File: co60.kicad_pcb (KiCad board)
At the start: 2 copper layers, 285 x 95.1 mm, 251 parts, among them J1 Conn_01x06, Q1 PZT2222A, SW1 SW_Push, U1 ATMEGA32U4, Y1 16MHz

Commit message: Update: Move some components on PCB
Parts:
- moved D14 1.33 mm to (344.7, 57.1)
- moved D1 0.78 mm to (84.8, 55.9)
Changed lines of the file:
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@@
   )
   (module Diodes_SMD:D_SOD-123 (layer B.Cu)
-    (at 344.090625 55.959375 90)
+    (at 344.678 57.15 90)
     (descr SOD-123)
     (tags SOD-123)
@@
   )
   (module Diodes_SMD:D_SOD-123 (layer B.Cu)
-    (at 84.9 55.1)
-    (descr SOD-123)
-    (tags SOD-123)
+    (at 84.836 55.88)
+    (descr SOD-123)
+    (tags SOD-123)

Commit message: Update: Rename some components
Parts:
- renumbered R_MCU_3 to RC2, R_MCU_4 to RC3, R_USB_1 to RC4, R_USB_2 to RC5, R_USB_3 to RC6, R_USB_4 to RC7
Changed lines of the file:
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@@
   (net 98 "Net-(Q1-Pad1)")
   (net 99 LEDPWM)
-  (net 100 "Net-(R_MCU_3-Pad1)")
+  (net 100 "Net-(RC2-Pad1)")
   (net 101 D_PLUS)
   (net 102 D_MINUS)
@@
   (net 176 "Net-(K_\\1-Pad4)")
   (net 177 "Net-(K_]1-Pad4)")
-  (net 178 "Net-(R_USB_3-Pad2)")
-  (net 179 "Net-(R_USB_4-Pad2)")
+  (net 178 "Net-(RC6-Pad2)")
+  (net 179 "Net-(RC7-Pad2)")
   (net 180 "Net-(USB1-PadB8)")
   (net 181 "Net-(USB1-PadB10)")
@@
     (add_net "Net-(K_]1-Pad4)")
     (add_net "Net-(Q1-Pad1)")
-    (add_net "Net-(R_MCU_3-Pad1)")
-    (add_net "Net-(R_USB_3-Pad2)")
-    (add_net "Net-(R_USB_4-Pad2)")
+    (add_net "Net-(RC2-Pad1)")
+    (add_net "Net-(RC6-Pad2)")
+    (add_net "Net-(RC7-Pad2)")
     (add_net "Net-(U1-Pad36)")
     (add_net "Net-(U1-Pad37)")
@@
       (net 1 GND))
     (pad B5 smd rect (at 0.5 -1.04) (size 0.3 0.7) (layers B.Cu B.Paste B.Mask)
-      (net 179 "Net-(R_USB_4-Pad2)"))
+      (net 179 "Net-(RC7-Pad2)"))
     (pad B4 smd rect (at 1 -1.04) (size 0.3 0.7) (layers B.Cu B.Paste B.Mask)
       (net 110 "Net-(DP1-Pad4)"))
@@
       (net 79 "Net-(DP1-Pad2)"))
     (pad A5 smd rect (at -0.75 0.66) (size 0.3 0.7) (layers B.Cu B.Paste B.Mask)
-      (net 178 "Net-(R_USB_3-Pad2)"))
+      (net 178 "Net-(RC6-Pad2)"))
     (pad A10 smd rect (at 1.75 0.66) (size 0.3 0.7) (layers B.Cu B.Paste B.Mask)
       (net 186 "Net-(USB1-PadA10)"))
@@
       (net 84 COL3))
     (pad 33 smd oval (at 5.715 4.0005 270) (size 1.89992 0.4064) (layers B.Cu B.Paste B.Mask)
-      (net 100 "Net-(R_MCU_3-Pad1)"))
+      (net 100 "Net-(RC2-Pad1)"))
     (pad 1 smd oval (at -5.715 4.0005 270) (size 1.89992 0.4064) (layers B.Cu B.Paste B.Mask)
       (net 83 COL2))
@@
     (tags "resistor 0603")
     (attr smd)
-    (fp_text reference R_USB_4 (at 0 1.45 90) (layer B.SilkS)
+    (fp_text reference RC7 (at 0 1.45 90) (layer B.SilkS)
       (effects (font (size 1 1) (thickness 0.15)) (justify mirror))
     )
@@
       (net 1 GND))
     (pad 2 smd rect (at 0.75 0 90) (size 0.5 0.9) (layers B.Cu B.Paste B.Mask)
-      (net 179 "Net-(R_USB_4-Pad2)"))
+      (net 179 "Net-(RC7-Pad2)"))
     (model ${KISYS3DMOD}/Resistors_SMD.3dshapes/R_0603.wrl
       (at (xyz 0 0 0))
@@
     (tags "resistor 0603")
     (attr smd)
-    (fp_text reference R_USB_3 (at 0 1.45 270) (layer B.SilkS)
+    (fp_text reference RC6 (at 0 1.45 270) (layer B.SilkS)
       (effects (font (size 1 1) (thickness 0.15)) (justify mirror))
     )
@@
       (net 1 GND))
     (pad 2 smd rect (at 0.75 0 270) (size 0.5 0.9) (layers B.Cu B.Paste B.Mask)
-      (net 178 "Net-(R_USB_3-Pad2)"))
+      (net 178 "Net-(RC6-Pad2)"))
     (model ${KISYS3DMOD}/Resistors_SMD.3dshapes/R_0603.wrl
       (at (xyz 0 0 0))
@@
     (tags "resistor 0603")
     (attr smd)
-    (fp_text reference R_USB_2 (at 0 1.45 90) (layer B.SilkS)
+    (fp_text reference RC5 (at 0 1.45 90) (layer B.SilkS)
       (effects (font (size 1 1) (thickness 0.15)) (justify mirror))
     )
@@
     (tags "resistor 0603")
     (attr smd)
-    (fp_text reference R_USB_1 (at 0 1.45 90) (layer B.SilkS)
+    (fp_text reference RC4 (at 0 1.45 90) (layer B.SilkS)
       (effects (font (size 1 1) (thickness 0.15)) (justify mirror))
     )
@@
     (tags "resistor 0603")
     (attr smd)
-    (fp_text reference R_MCU_4 (at 0 1.45) (layer B.SilkS)
+    (fp_text reference RC3 (at 0 1.45) (layer B.SilkS)
       (effects (font (size 1 1) (thickness 0.15)) (justify mirror))
     )
@@
     (tags "resistor 0603")
     (attr smd)
-    (fp_text reference R_MCU_3 (at 0 1.45 180) (layer B.SilkS)
+    (fp_text reference RC2 (at 0 1.45 180) (layer B.SilkS)
       (effects (font (size 1 1) (thickness 0.15)) (justify mirror))
     )
@@
     (fp_line (start 1.25 -0.7) (end -1.25 -0.7) (layer B.CrtYd) (width 0.05))
     (pad 1 smd rect (at -0.75 0 180) (size 0.5 0.9) (layers B.Cu B.Paste B.Mask)
-      (net 100 "Net-(R_MCU_3-Pad1)"))
+      (net 100 "Net-(RC2-Pad1)"))
     (pad 2 smd rect (at 0.75 0 180) (size 0.5 0.9) (layers B.Cu B.Paste B.Mask)
       (net 1 GND))

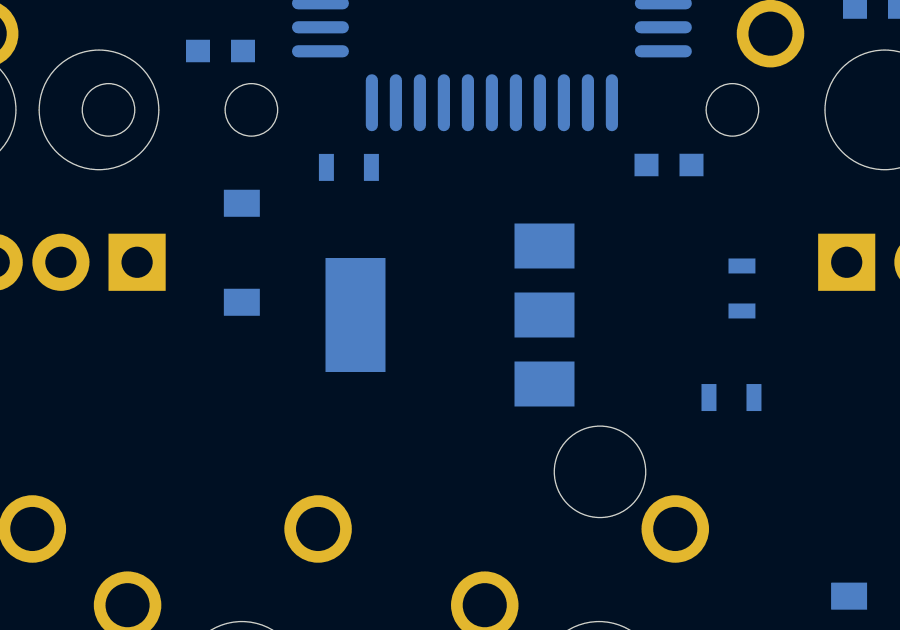
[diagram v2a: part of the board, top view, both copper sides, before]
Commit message: Update: Switch transistor to something smaller
I don't think I needed a transistor as big as I had for the
LEDs. I've switched to a SOT-23 footprint BJT that can
dissipate 500 mW. This should be more than enough for
68 LEDs at 5 mA each.
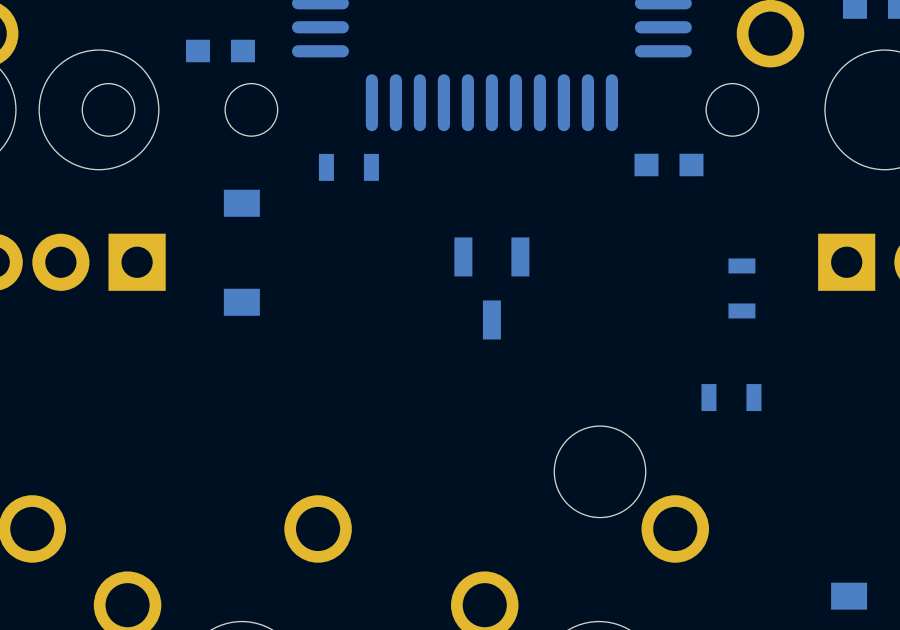
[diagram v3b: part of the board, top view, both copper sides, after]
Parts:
- Q1: value PZT2222A -> FMMT493TA; footprint TO_SOT_Packages_SMD:SOT-223 -> digikey-footprints:SOT-23-3
- moved Q1 1.65 mm to (108.3, 106.0), turned to 270 degrees
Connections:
- Q1 pad 1: Net-(Q1-Pad1) -> GND
- Q1 pad 2: LEDGND -> Net-(Q1-Pad2)
- Q1 pad 3: GND -> LEDGND
- RC1 pad 1: Net-(Q1-Pad1) -> Net-(Q1-Pad2)

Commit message: Update: More PCB component adjustment
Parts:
- K_LCTL1: footprint MX_Alps_Hybrid:MXOnly-1.25U -> MX_Alps_Hybrid:MXOnly-1.25U-FLIPPED
- K_LCTL2: footprint MX_Alps_Hybrid:MXOnly-1.5U-FLIPPED -> MX_Alps_Hybrid:MXOnly-1.5U
- moved C8 4.97 mm to (98.8, 88.1), turned to 90 degrees
- moved C3 2.50 mm to (109.5, 84.5), turned to 90 degrees
- moved C5 1.70 mm to (98.8, 91.7), turned to 270 degrees
- moved RC2 1.65 mm to (103.6, 103.6)
- moved R30 1.19 mm to (86.9, 103.6)
- moved C4 0.77 mm to (118.1, 90.4)
- moved RC3 0.70 mm to (115.6, 88.4)
- moved C6 0.64 mm to (98.8, 97.6)
- moved USB1 0.14 mm to (97.2, 59.7)

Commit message: Update: Reverse crystal connections
I'm not sure if this matters or not, but it seems
consistent with the way the GH60 does it.
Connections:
- U1 pad 16: Net-(C1-Pad1) -> Net-(C2-Pad1)
- U1 pad 17: Net-(C2-Pad1) -> Net-(C1-Pad1)
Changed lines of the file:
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@@
       (net 5 VCC))
     (pad 17 smd oval (at 0 -5.715 270) (size 0.4064 1.89992) (layers B.Cu B.Paste B.Mask)
+      (net 2 "Net-(C1-Pad1)"))
+    (pad 16 smd oval (at -0.8001 -5.715 270) (size 0.4064 1.89992) (layers B.Cu B.Paste B.Mask)
       (net 3 "Net-(C2-Pad1)"))
-    (pad 16 smd oval (at -0.8001 -5.715 270) (size 0.4064 1.89992) (layers B.Cu B.Paste B.Mask)
-      (net 2 "Net-(C1-Pad1)"))
     (pad 15 smd oval (at -1.6002 -5.715 270) (size 0.4064 1.89992) (layers B.Cu B.Paste B.Mask)
       (net 1 GND))

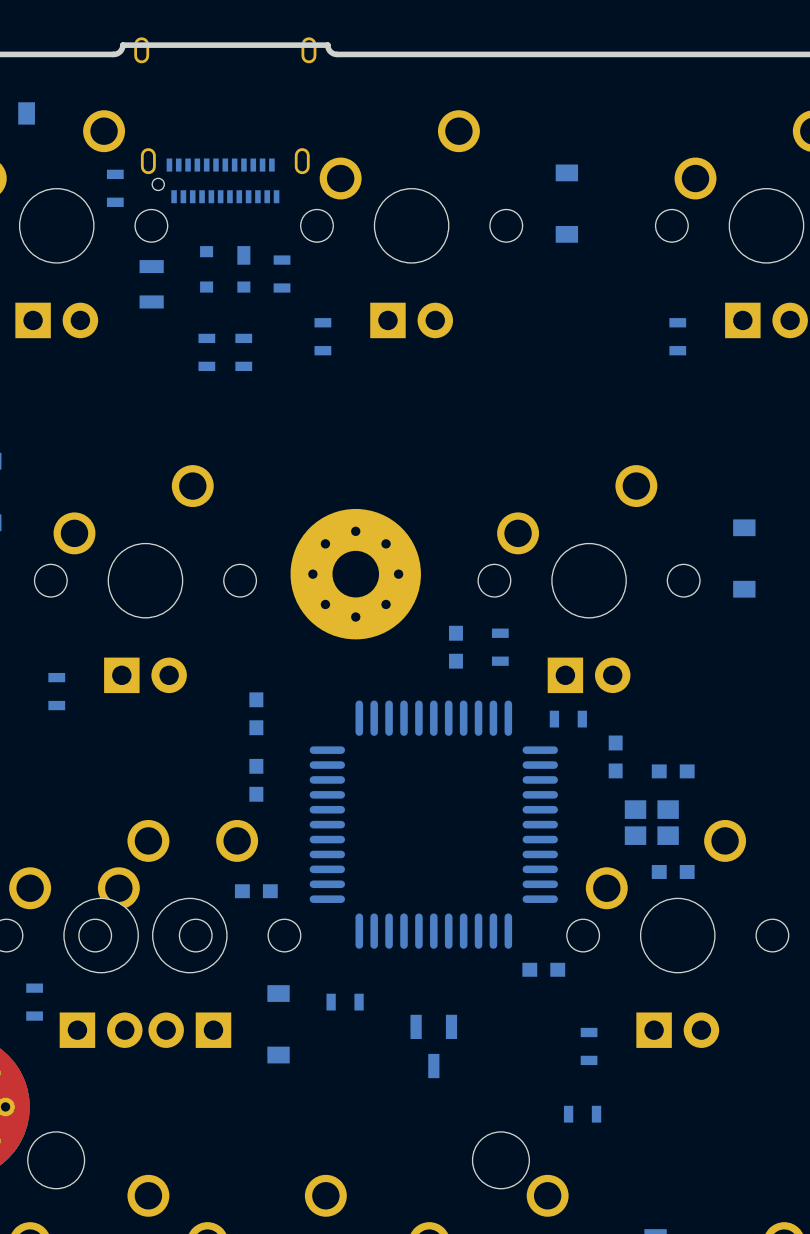
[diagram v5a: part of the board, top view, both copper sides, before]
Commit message: Update: Begin routing PCB
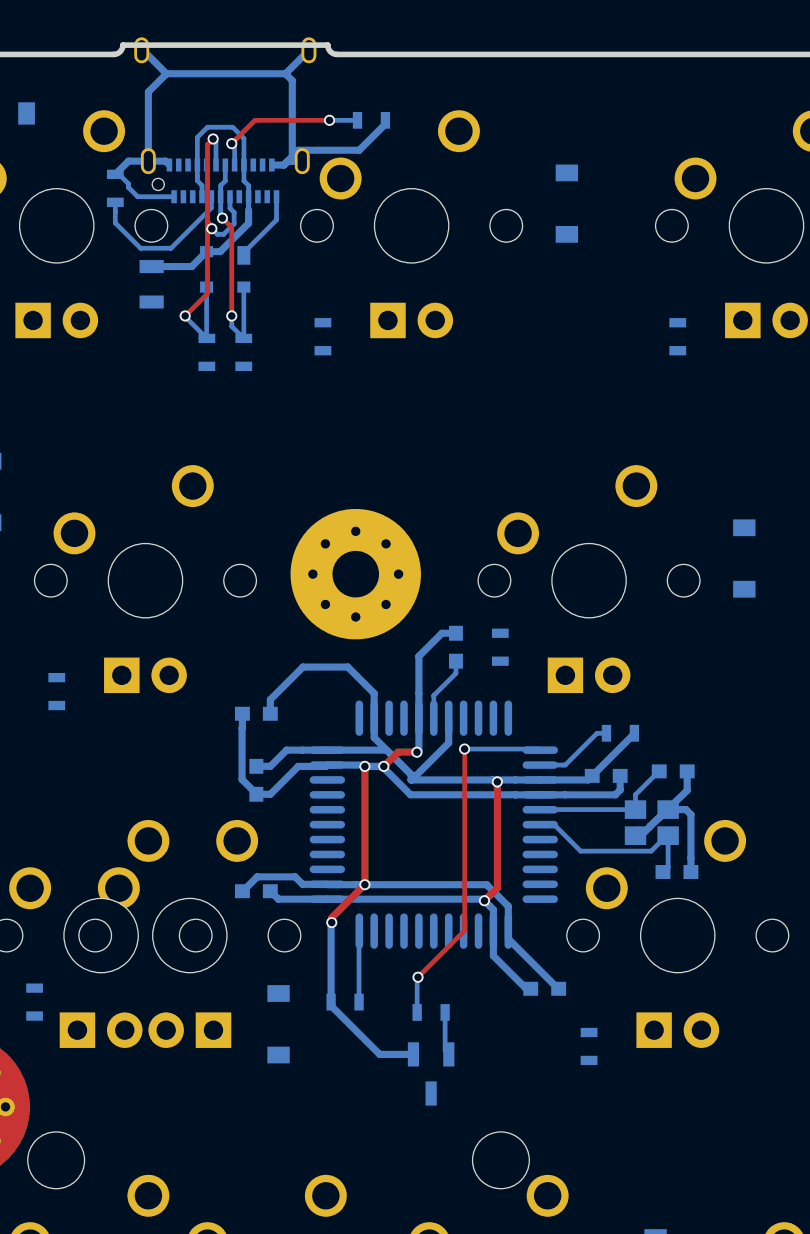
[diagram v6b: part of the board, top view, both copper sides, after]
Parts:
- moved RC1 9.79 mm to (108.2, 104.1), turned to 180 degrees
- moved RC7 9.54 mm to (105.0, 56.2), turned to 180 degrees
- moved RC3 2.90 mm to (118.4, 89.2), turned to 180 degrees
- moved Q1 1.48 mm to (108.2, 107.4)
- moved C4 1.14 mm to (117.6, 91.4), turned to 0 degrees
- moved C7 1.02 mm to (114.3, 102.9)
- moved C1 0.20 mm to (121.4, 96.6)
- turned C8 to 180 degrees
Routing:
- net GND: track 0.00 -> 127.0 mm, vias 0 -> 5
- net VCC: track 0.00 -> 64.4 mm, vias 0 -> 2
- net Net-(DP1-Pad3): track 0.00 -> 19.7 mm, vias 0 -> 3
- net LEDPWM: track 0.00 -> 19.3 mm, vias 0 -> 2
- net Net-(DP1-Pad4): track 0.00 -> 17.8 mm
- net Net-(DP1-Pad2): track 0.00 -> 12.7 mm, vias 0 -> 2
- net Net-(C1-Pad1): track 0.00 -> 9.86 mm
- net Net-(RC7-Pad2): track 0.00 -> 8.48 mm, vias 0 -> 2
- net Net-(RC6-Pad2): track 0.00 -> 8.33 mm
- net Net-(C2-Pad1): track 0.00 -> 7.71 mm
- net Net-(J1-Pad2): track 0.00 -> 5.01 mm
- net Net-(RC2-Pad1): track 0.00 -> 3.81 mm
- net Net-(C3-Pad1): track 0.00 -> 3.55 mm
- net Net-(Q1-Pad2): track 0.00 -> 2.33 mm

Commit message: Update: More work on PCB routing
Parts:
- moved RC4 0.86 mm to (99.0, 68.8)
- moved RC5 0.67 mm to (95.5, 68.8)
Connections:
- net D_MINUS renamed D_N
- net D_PLUS renamed D_P
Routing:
- net GND: track 127.0 -> 153.2 mm, vias 5 -> 7
- net D_N: track 0.00 -> 25.5 mm, vias 0 -> 2
- net D_P: track 0.00 -> 23.8 mm, vias 0 -> 2
- net VCC: track 64.4 -> 87.4 mm, vias 2 -> 4
- net Net-(DP1-Pad3): track 19.7 -> 18.3 mm, vias 3 -> 4

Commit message: Update: More routing
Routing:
- net D_P: track 23.8 -> 27.0 mm
- net GND: track 153.2 -> 153.9 mm
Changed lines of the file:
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@@
   (general
     (links 572)
-    (no_connects 501)
+    (no_connects 499)
     (area 0 0 0 0)
     (thickness 1.6)
     (drawings 0)
-    (tracks 286)
+    (tracks 299)
     (zones 0)
     (modules 251)
@@
     (pad "" np_thru_hole circle (at 5.08 0 48.0996) (size 1.75 1.75) (drill 1.75) (layers *.Cu *.Mask))
   )
+  (segment (start 109.5375 83.784375) (end 107.546775 83.784375) (width 0.381) (layer B.Cu) (net 1))
+  (segment (start 107.546775 83.784375) (end 107.546775 87.013415) (width 0.381) (layer B.Cu) (net 1))
+  (segment (start 107.546775 87.013415) (end 107.546775 88.344375) (width 0.381) (layer B.Cu) (net 1))
   (segment (start 109.5 82) (end 109.5 83.746875) (width 0.381) (layer B.Cu) (net 1))
   (segment (start 109.5 83.746875) (end 109.5375 83.784375) (width 0.381) (layer B.Cu) (net 1))
@@
   (segment (start 104.574975 90.858975) (end 104.648 90.932) (width 0.381) (layer B.Cu) (net 1))
   (via (at 104.648 90.932) (size 0.6) (drill 0.4) (layers F.Cu B.Cu) (net 1))
-  (segment (start 109.5375 83.784375) (end 108.7815 83.784375) (width 0.381) (layer B.Cu) (net 1))
-  (segment (start 108.7815 83.784375) (end 107.546775 85.0191) (width 0.381) (layer B.Cu) (net 1))
-  (segment (start 107.546775 85.0191) (end 107.546775 87.013415) (width 0.381) (layer B.Cu) (net 1))
-  (segment (start 107.546775 87.013415) (end 107.546775 88.344375) (width 0.381) (layer B.Cu) (net 1))
   (segment (start 102.55885 90.932) (end 102.631875 90.858975) (width 0.381) (layer B.Cu) (net 1))
   (segment (start 98.071875 88.10625) (end 98.071875 88.165875) (width 0.381) (layer B.Cu) (net 1))
@@
   (segment (start 108.346875 87.129) (end 108.346875 87.140415) (width 0.254) (layer B.Cu) (net 4))
   (segment (start 108.346875 87.140415) (end 108.346875 88.344375) (width 0.254) (layer B.Cu) (net 4))
+  (segment (start 99.217451 80.353523) (end 99.217451 85.543187) (width 0.381) (layer F.Cu) (net 5))
+  (segment (start 93.25 71.382989) (end 98.772078 76.905067) (width 0.381) (layer F.Cu) (net 5))
+  (segment (start 99.217451 85.543187) (end 99.25 85.575736) (width 0.381) (layer F.Cu) (net 5))
+  (segment (start 93.25 67.75) (end 93.25 71.382989) (width 0.381) (layer F.Cu) (net 5))
+  (segment (start 99.25 85.575736) (end 99.25 86) (width 0.381) (layer F.Cu) (net 5))
+  (segment (start 98.772078 79.90815) (end 99.217451 80.353523) (width 0.381) (layer F.Cu) (net 5))
+  (segment (start 98.772078 76.905067) (end 98.772078 79.90815) (width 0.381) (layer F.Cu) (net 5))
   (segment (start 99.25 86) (end 99.25 87.784375) (width 0.381) (layer B.Cu) (net 5))
   (segment (start 99.25 87.784375) (end 99.571875 88.10625) (width 0.381) (layer B.Cu) (net 5))
-  (segment (start 93.25 70.5) (end 99.25 76.5) (width 0.381) (layer F.Cu) (net 5))
-  (segment (start 99.25 76.5) (end 99.25 86) (width 0.381) (layer F.Cu) (net 5))
   (via (at 99.25 86) (size 0.6) (drill 0.4) (layers F.Cu B.Cu) (net 5))
-  (segment (start 93.25 67.75) (end 93.25 70.5) (width 0.381) (layer F.Cu) (net 5))
   (segment (start 93.2 66) (end 93.2 67.7) (width 0.381) (layer B.Cu) (net 5))
   (segment (start 93.2 67.7) (end 93.25 67.75) (width 0.381) (layer B.Cu) (net 5))
@@
   (segment (start 108.954 104.14) (end 108.954 106.192) (width 0.254) (layer B.Cu) (net 187))
   (segment (start 108.954 106.192) (end 109.154 106.392) (width 0.254) (layer B.Cu) (net 187))
+  (segment (start 102.317441 84.443351) (end 103.193351 84.443351) (width 0.254) (layer F.Cu) (net 188))
+  (segment (start 107.987101 84.762899) (end 106.75 86) (width 0.254) (layer F.Cu) (net 188))
+  (segment (start 103.193351 84.443351) (end 103.512899 84.762899) (width 0.254) (layer F.Cu) (net 188))
+  (segment (start 99.75 79.503084) (end 100.195373 79.948456) (width 0.254) (layer F.Cu) (net 188))
+  (segment (start 100.325399 81.575399) (end 100.325399 82.451309) (width 0.254) (layer F.Cu) (net 188))
+  (segment (start 100.195373 79.948456) (end 100.195373 81.445373) (width 0.254) (layer F.Cu) (net 188))
+  (segment (start 99.75 70.75) (end 99.75 79.503084) (width 0.254) (layer F.Cu) (net 188))
+  (segment (start 100.195373 81.445373) (end 100.325399 81.575399) (width 0.254) (layer F.Cu) (net 188))
+  (segment (start 100.325399 82.451309) (end 102.317441 84.443351) (width 0.254) (layer F.Cu) (net 188))
+  (segment (start 103.512899 84.762899) (end 107.987101 84.762899) (width 0.254) (layer F.Cu) (net 188))
   (segment (start 106.75 86) (end 106.75 88.34105) (width 0.254) (layer B.Cu) (net 188))
   (segment (start 106.75 88.34105) (end 106.746675 88.344375) (width 0.254) (layer B.Cu) (net 188))
-  (segment (start 99.75 70.75) (end 107.987101 78.987101) (width 0.254) (layer F.Cu) (net 188))
-  (segment (start 107.987101 78.987101) (end 107.987101 84.762899) (width 0.254) (layer F.Cu) (net 188))
-  (segment (start 107.987101 84.762899) (end 106.75 86) (width 0.254) (layer F.Cu) (net 188))
   (via (at 106.75 86) (size 0.6) (drill 0.4) (layers F.Cu B.Cu) (net 188))
   (segment (start 99 69.5) (end 99 70) (width 0.254) (layer B.Cu) (net 188))
@@
   (via (at 99.75 70.75) (size 0.6) (drill 0.4) (layers F.Cu B.Cu) (net 188))
   (segment (start 106.746675 87.597615) (end 106.746675 88.344375) (width 0.254) (layer B.Cu) (net 188))
+  (segment (start 102.727497 85.5) (end 105.575736 85.5) (width 0.254) (layer F.Cu) (net 189))
+  (segment (start 96.25 70.75) (end 99.292789 73.792789) (width 0.254) (layer F.Cu) (net 189))
+  (segment (start 99.738162 80.137838) (end 99.738162 82.510665) (width 0.254) (layer F.Cu) (net 189))
+  (segment (start 99.292789 73.792789) (end 99.292789 79.692465) (width 0.254) (layer F.Cu) (net 189))
+  (segment (start 99.292789 79.692465) (end 99.738162 80.137838) (width 0.254) (layer F.Cu) (net 189))
+  (segment (start 99.738162 82.510665) (end 102.727497 85.5) (width 0.254) (layer F.Cu) (net 189))
+  (segment (start 105.575736 85.5) (end 106 85.5) (width 0.254) (layer F.Cu) (net 189))
   (segment (start 106 85.5) (end 106 88.29095) (width 0.254) (layer B.Cu) (net 189))
   (segment (start 106 88.29095) (end 105.946575 88.344375) (width 0.254) (layer B.Cu) (net 189))
-  (segment (start 96.25 70.75) (end 100.325399 74.825399) (width 0.254) (layer F.Cu) (net 189))
-  (segment (start 100.325399 74.825399) (end 100.325399 82.451309) (width 0.254) (layer F.Cu) (net 189))
-  (segment (start 100.325399 82.451309) (end 103.37409 85.5) (width 0.254) (layer F.Cu) (net 189))
-  (segment (start 103.37409 85.5) (end 106 85.5) (width 0.254) (layer F.Cu) (net 189))
   (via (at 106 85.5) (size 0.6) (drill 0.4) (layers F.Cu B.Cu) (net 189))
   (segment (start 95.5 69.5) (end 95.5 70) (width 0.254) (layer B.Cu) (net 189))
